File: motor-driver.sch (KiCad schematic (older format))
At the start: 9 parts, among them U3 A3950SLP-T

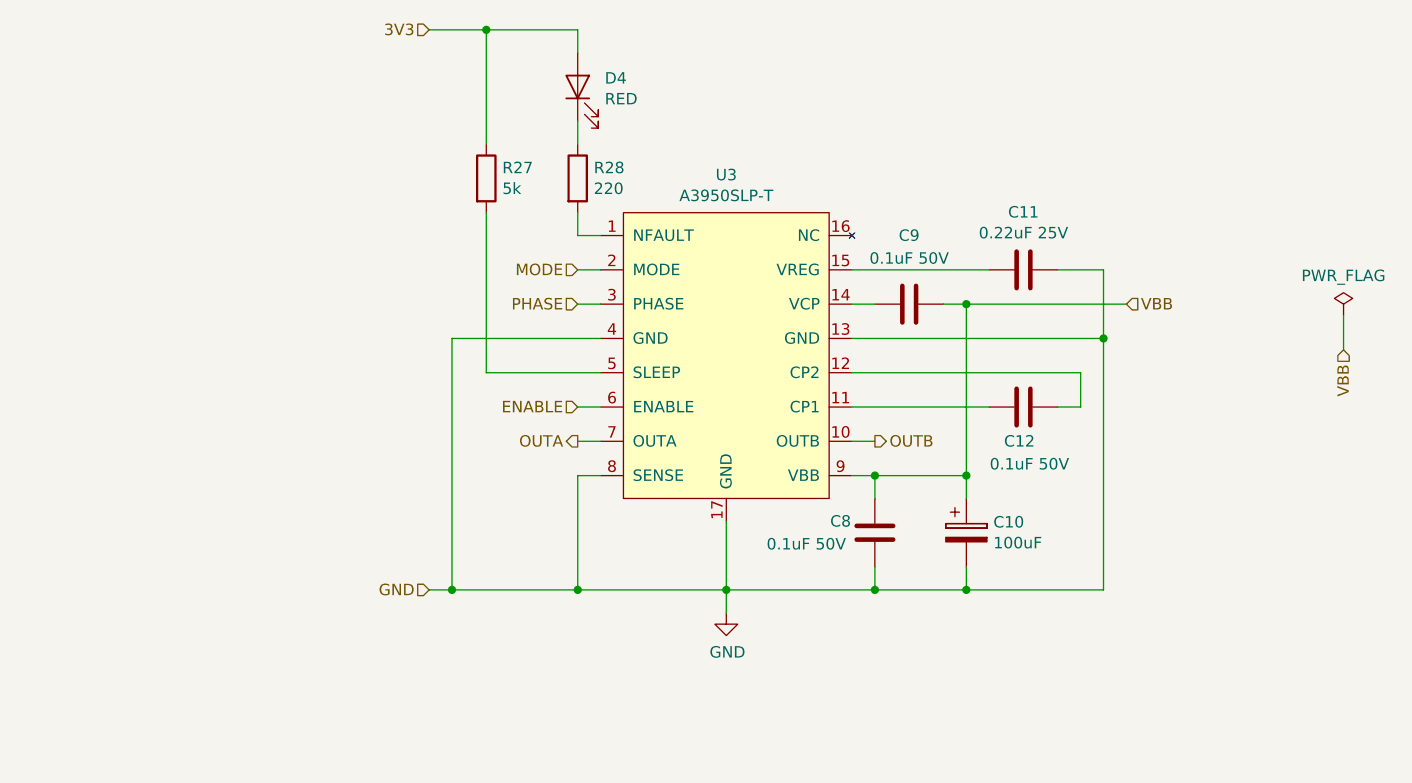
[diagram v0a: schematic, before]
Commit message: Generated annotations, netlists and assigned footprints into components
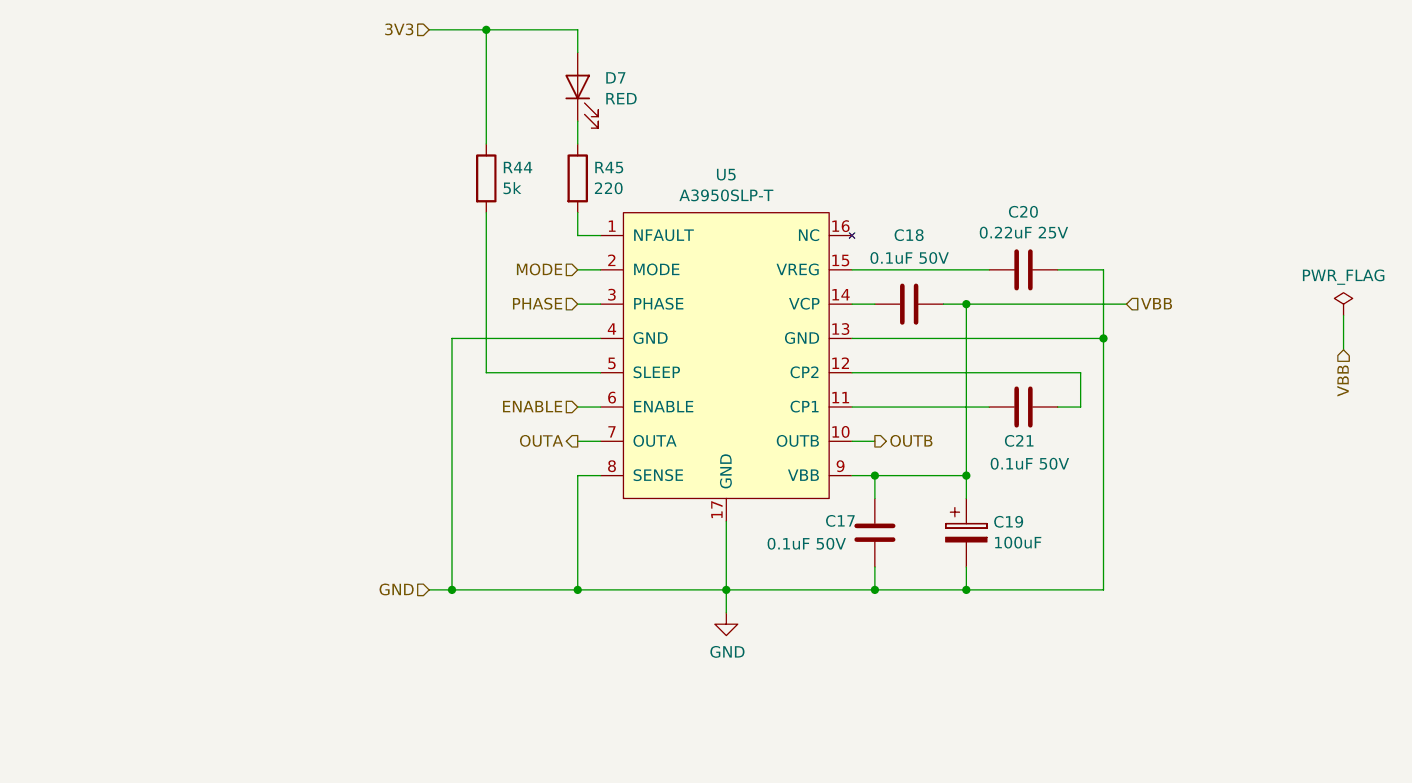
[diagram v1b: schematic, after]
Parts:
- C10: footprint (none) -> Capacitor_SMD:CP_Elec_8x10.5
- C11: footprint (none) -> Capacitor_SMD:C_0603_1608Metric_Pad1.05x0.95mm_HandSolder
- C12, C8, C9: footprint (none) -> Capacitor_SMD:C_0805_2012Metric_Pad1.15x1.40mm_HandSolder
- D4: footprint (none) -> LED_SMD:LED_0603_1608Metric_Pad1.05x0.95mm_HandSolder
- R27, R28: footprint (none) -> Resistor_SMD:R_0805_2012Metric_Pad1.15x1.40mm_HandSolder
- U3: footprint (none) -> Package_SO:HTSSOP-16-1EP_4.4x5mm_P0.65mm_EP3.4x5mm_Mask3x3mm_ThermalVias
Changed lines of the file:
@@
 AR Path="/5BF2FCBD/5BD9640D" Ref="U?"  Part="1"
 AR Path="/5C015BE4/5BD9640D" Ref="U5"  Part="1"
-F 0 "U3" H 6050 4415 50  0000 C CNN
+F 0 "U5" H 6050 4415 50  0000 C CNN
 F 1 "A3950SLP-T" H 6050 4324 50  0000 C CNN
-F 2 "" H 6100 4300 50  0001 C CNN
+F 2 "Package_SO:HTSSOP-16-1EP_4.4x5mm_P0.65mm_EP3.4x5mm_Mask3x3mm_ThermalVias" H 6100 4300 50  0001 C CNN
 F 3 "" H 6100 4300 50  0001 C CNN
 	1    5800 3600
@@
 AR Path="/5BF2FCBD/5BDA6B35" Ref="C?"  Part="1"
 AR Path="/5C015BE4/5BDA6B35" Ref="C17"  Part="1"
-F 0 "C8" H 6550 4400 50  0000 C CNN
+F 0 "C17" H 6550 4400 50  0000 C CNN
 F 1 "0.1uF 50V" H 6400 4300 50  0000 C CNN
-F 2 "" H 6738 4200 50  0001 C CNN
+F 2 "Capacitor_SMD:C_0805_2012Metric_Pad1.15x1.40mm_HandSolder" H 6738 4200 50  0001 C CNN
 F 3 "~" H 6700 4350 50  0001 C CNN
 F 4 "50V" V 6700 4350 50  0001 C CNN "Voltage"
@@
 AR Path="/5BF2FCBD/5BDBEA6E" Ref="C?"  Part="1"
 AR Path="/5C015BE4/5BDBEA6E" Ref="C21"  Part="1"
-F 0 "C12" V 7200 3750 50  0000 L CNN
+F 0 "C21" V 7200 3750 50  0000 L CNN
 F 1 "0.1uF 50V" V 7100 3600 50  0000 L CNN
-F 2 "" H 7388 3650 50  0001 C CNN
+F 2 "Capacitor_SMD:C_0805_2012Metric_Pad1.15x1.40mm_HandSolder" H 7388 3650 50  0001 C CNN
 F 3 "~" H 7350 3800 50  0001 C CNN
 	1    7350 3800
@@
 AR Path="/5BF2FCBD/5BDD7CCD" Ref="C?"  Part="1"
 AR Path="/5C015BE4/5BDD7CCD" Ref="C18"  Part="1"
-F 0 "C9" V 6550 3350 50  0000 C CNN
+F 0 "C18" V 6550 3350 50  0000 C CNN
 F 1 "0.1uF 50V" V 6650 3350 50  0000 C CNN
-F 2 "" H 6888 3200 50  0001 C CNN
+F 2 "Capacitor_SMD:C_0805_2012Metric_Pad1.15x1.40mm_HandSolder" H 6888 3200 50  0001 C CNN
 F 3 "~" H 6850 3350 50  0001 C CNN
 	1    6850 3350
@@
 AR Path="/5BF2FCBD/5BDE6995" Ref="C?"  Part="1"
 AR Path="/5C015BE4/5BDE6995" Ref="C19"  Part="1"
-F 0 "C10" H 7218 4396 50  0000 L CNN
+F 0 "C19" H 7218 4396 50  0000 L CNN
 F 1 "100uF" H 7218 4305 50  0000 L CNN
-F 2 "" H 7138 4200 50  0001 C CNN
+F 2 "Capacitor_SMD:CP_Elec_8x10.5" H 7138 4200 50  0001 C CNN
 F 3 "~" H 7100 4350 50  0001 C CNN
 	1    7100 4350
@@
 AR Path="/5BF2FCBD/5BDFF4AF" Ref="C?"  Part="1"
 AR Path="/5C015BE4/5BDFF4AF" Ref="C20"  Part="1"
-F 0 "C11" V 7098 3200 50  0000 C CNN
+F 0 "C20" V 7098 3200 50  0000 C CNN
 F 1 "0.22uF 25V" V 7189 3200 50  0000 C CNN
-F 2 "" H 7388 3050 50  0001 C CNN
+F 2 "Capacitor_SMD:C_0603_1608Metric_Pad1.05x0.95mm_HandSolder" H 7388 3050 50  0001 C CNN
 F 3 "~" H 7350 3200 50  0001 C CNN
 	1    7350 3200
@@
 AR Path="/5BF2FCBD/5BE2A012" Ref="R?"  Part="1"
 AR Path="/5C015BE4/5BE2A012" Ref="R44"  Part="1"
-F 0 "R27" H 5070 2846 50  0000 L CNN
+F 0 "R44" H 5070 2846 50  0000 L CNN
 F 1 "5k" H 5070 2755 50  0000 L CNN
-F 2 "" V 4930 2800 50  0001 C CNN
+F 2 "Resistor_SMD:R_0805_2012Metric_Pad1.15x1.40mm_HandSolder" V 4930 2800 50  0001 C CNN
 F 3 "~" H 5000 2800 50  0001 C CNN
 	1    5000 2800
@@
 AR Path="/5BF2FCBD/5BE427B2" Ref="D?"  Part="1"
 AR Path="/5C015BE4/5BE427B2" Ref="D7"  Part="1"
-F 0 "D4" V 5438 2282 50  0000 R CNN
+F 0 "D7" V 5438 2282 50  0000 R CNN
 F 1 "RED" V 5347 2282 50  0000 R CNN
-F 2 "" H 5400 2400 50  0001 C CNN
+F 2 "LED_SMD:LED_0603_1608Metric_Pad1.05x0.95mm_HandSolder" H 5400 2400 50  0001 C CNN
 F 3 "~" H 5400 2400 50  0001 C CNN
 	1    5400 2400
@@
 AR Path="/5BF2FCBD/5BE42954" Ref="R?"  Part="1"
 AR Path="/5C015BE4/5BE42954" Ref="R45"  Part="1"
-F 0 "R28" H 5470 2846 50  0000 L CNN
+F 0 "R45" H 5470 2846 50  0000 L CNN
 F 1 "220" H 5470 2755 50  0000 L CNN
-F 2 "" V 5330 2800 50  0001 C CNN
+F 2 "Resistor_SMD:R_0805_2012Metric_Pad1.15x1.40mm_HandSolder" V 5330 2800 50  0001 C CNN
 F 3 "~" H 5400 2800 50  0001 C CNN
 	1    5400 2800

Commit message: Added power supply section to PCB. Added missing components footprints.
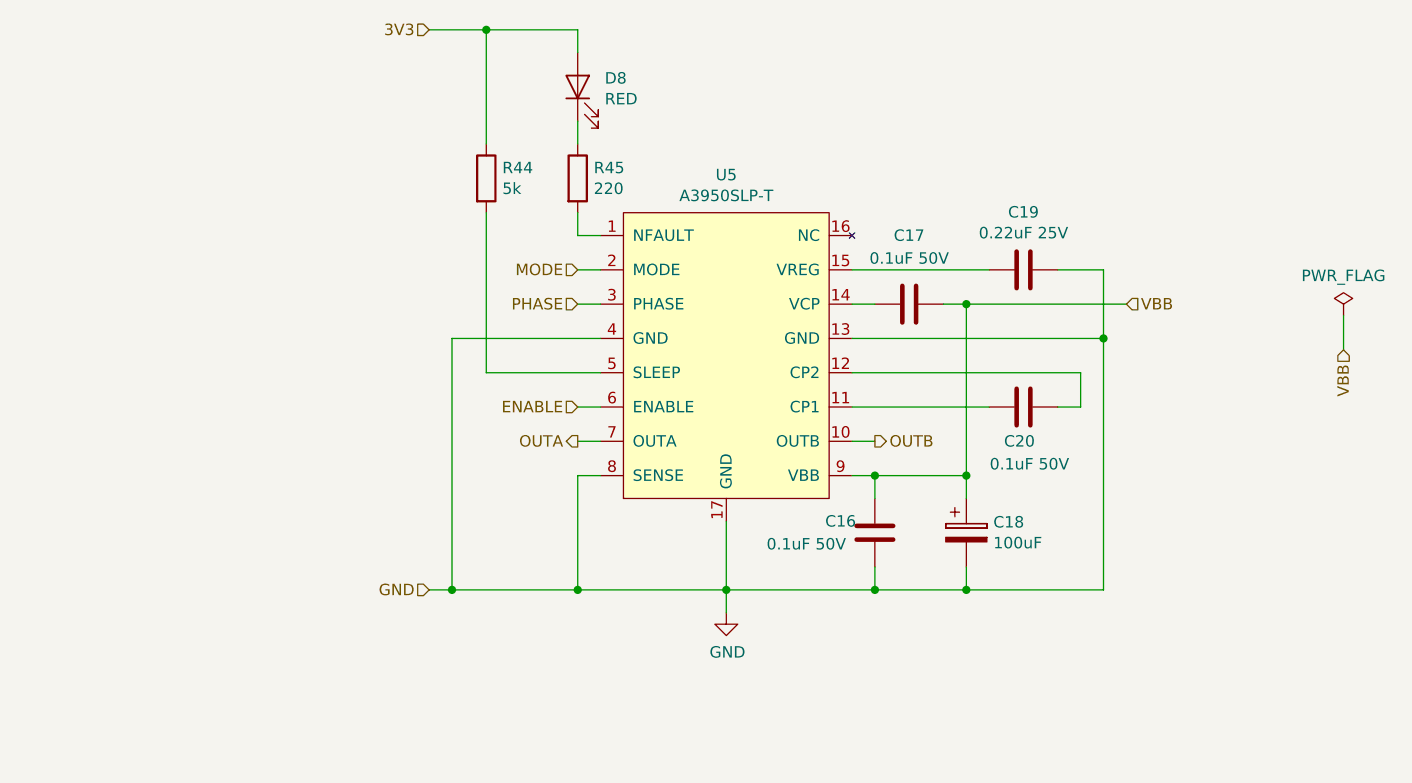
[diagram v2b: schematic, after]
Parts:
- renumbered C11 to C10, C12 to C11, C8 to C7, C9 to C8, C10 to C9, D4 to D5
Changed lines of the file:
@@
 $EndComp
 $Comp
-L power:GND #PWR017
+L power:GND #PWR010
 U 1 1 5BD9C7A2
 P 6050 4700
-AR Path="/5BDB64FF/5BD9C7A2" Ref="#PWR017"  Part="1"
+AR Path="/5BDB64FF/5BD9C7A2" Ref="#PWR010"  Part="1"
 AR Path="/5BF2FCBD/5BD9C7A2" Ref="#PWR?"  Part="1"
-AR Path="/5C015BE4/5BD9C7A2" Ref="#PWR023"  Part="1"
-F 0 "#PWR023" H 6050 4450 50  0001 C CNN
+AR Path="/5C015BE4/5BD9C7A2" Ref="#PWR014"  Part="1"
+F 0 "#PWR014" H 6050 4450 50  0001 C CNN
 F 1 "GND" H 6055 4527 50  0000 C CNN
 F 2 "" H 6050 4700 50  0001 C CNN
@@
 	5400 4600 4850 4600
 $Comp
-L Device:C C8
+L Device:C C7
 U 1 1 5BDA6B35
 P 6700 4350
-AR Path="/5BDB64FF/5BDA6B35" Ref="C8"  Part="1"
+AR Path="/5BDB64FF/5BDA6B35" Ref="C7"  Part="1"
 AR Path="/5BF2FCBD/5BDA6B35" Ref="C?"  Part="1"
-AR Path="/5C015BE4/5BDA6B35" Ref="C17"  Part="1"
-F 0 "C17" H 6550 4400 50  0000 C CNN
+AR Path="/5C015BE4/5BDA6B35" Ref="C16"  Part="1"
+F 0 "C16" H 6550 4400 50  0000 C CNN
 F 1 "0.1uF 50V" H 6400 4300 50  0000 C CNN
 F 2 "Capacitor_SMD:C_0805_2012Metric_Pad1.15x1.40mm_HandSolder" H 6738 4200 50  0001 C CNN
@@
 	6600 4100 6700 4100
 $Comp
-L Device:C C12
+L Device:C C11
 U 1 1 5BDBEA6E
 P 7350 3800
-AR Path="/5BDB64FF/5BDBEA6E" Ref="C12"  Part="1"
+AR Path="/5BDB64FF/5BDBEA6E" Ref="C11"  Part="1"
 AR Path="/5BF2FCBD/5BDBEA6E" Ref="C?"  Part="1"
-AR Path="/5C015BE4/5BDBEA6E" Ref="C21"  Part="1"
-F 0 "C21" V 7200 3750 50  0000 L CNN
+AR Path="/5C015BE4/5BDBEA6E" Ref="C20"  Part="1"
+F 0 "C20" V 7200 3750 50  0000 L CNN
 F 1 "0.1uF 50V" V 7100 3600 50  0000 L CNN
 F 2 "Capacitor_SMD:C_0805_2012Metric_Pad1.15x1.40mm_HandSolder" H 7388 3650 50  0001 C CNN
@@
 	6700 4600 6700 4500
 $Comp
-L Device:C C9
+L Device:C C8
 U 1 1 5BDD7CCD
 P 6850 3350
-AR Path="/5BDB64FF/5BDD7CCD" Ref="C9"  Part="1"
+AR Path="/5BDB64FF/5BDD7CCD" Ref="C8"  Part="1"
 AR Path="/5BF2FCBD/5BDD7CCD" Ref="C?"  Part="1"
-AR Path="/5C015BE4/5BDD7CCD" Ref="C18"  Part="1"
-F 0 "C18" V 6550 3350 50  0000 C CNN
+AR Path="/5C015BE4/5BDD7CCD" Ref="C17"  Part="1"
+F 0 "C17" V 6550 3350 50  0000 C CNN
 F 1 "0.1uF 50V" V 6650 3350 50  0000 C CNN
 F 2 "Capacitor_SMD:C_0805_2012Metric_Pad1.15x1.40mm_HandSolder" H 6888 3200 50  0001 C CNN
@@
 Connection ~ 6700 4600
 $Comp
-L Device:CP C10
+L Device:CP C9
 U 1 1 5BDE6995
 P 7100 4350
-AR Path="/5BDB64FF/5BDE6995" Ref="C10"  Part="1"
+AR Path="/5BDB64FF/5BDE6995" Ref="C9"  Part="1"
 AR Path="/5BF2FCBD/5BDE6995" Ref="C?"  Part="1"
-AR Path="/5C015BE4/5BDE6995" Ref="C19"  Part="1"
-F 0 "C19" H 7218 4396 50  0000 L CNN
+AR Path="/5C015BE4/5BDE6995" Ref="C18"  Part="1"
+F 0 "C18" H 7218 4396 50  0000 L CNN
 F 1 "100uF" H 7218 4305 50  0000 L CNN
 F 2 "Capacitor_SMD:CP_Elec_8x10.5" H 7138 4200 50  0001 C CNN
@@
 Connection ~ 7100 4600
 $Comp
-L Device:C C11
+L Device:C C10
 U 1 1 5BDFF4AF
 P 7350 3200
-AR Path="/5BDB64FF/5BDFF4AF" Ref="C11"  Part="1"
+AR Path="/5BDB64FF/5BDFF4AF" Ref="C10"  Part="1"
 AR Path="/5BF2FCBD/5BDFF4AF" Ref="C?"  Part="1"
-AR Path="/5C015BE4/5BDFF4AF" Ref="C20"  Part="1"
-F 0 "C20" V 7098 3200 50  0000 C CNN
+AR Path="/5C015BE4/5BDFF4AF" Ref="C19"  Part="1"
+F 0 "C19" V 7098 3200 50  0000 C CNN
 F 1 "0.22uF 25V" V 7189 3200 50  0000 C CNN
 F 2 "Capacitor_SMD:C_0603_1608Metric_Pad1.05x0.95mm_HandSolder" H 7388 3050 50  0001 C CNN
@@
 	5000 3650 5500 3650
 $Comp
-L Device:LED D4
+L Device:LED D5
 U 1 1 5BE427B2
 P 5400 2400
-AR Path="/5BDB64FF/5BE427B2" Ref="D4"  Part="1"
+AR Path="/5BDB64FF/5BE427B2" Ref="D5"  Part="1"
 AR Path="/5BF2FCBD/5BE427B2" Ref="D?"  Part="1"
-AR Path="/5C015BE4/5BE427B2" Ref="D7"  Part="1"
-F 0 "D7" V 5438 2282 50  0000 R CNN
+AR Path="/5C015BE4/5BE427B2" Ref="D8"  Part="1"
+F 0 "D8" V 5438 2282 50  0000 R CNN
 F 1 "RED" V 5347 2282 50  0000 R CNN
 F 2 "LED_SMD:LED_0603_1608Metric_Pad1.05x0.95mm_HandSolder" H 5400 2400 50  0001 C CNN
@@
 VBB
 $Comp
-L power:PWR_FLAG #FLG02
+L power:PWR_FLAG #FLG03
 U 1 1 5C04A11D
 P 8750 3400
-AR Path="/5BDB64FF/5C04A11D" Ref="#FLG02"  Part="1"
-AR Path="/5C015BE4/5C04A11D" Ref="#FLG03"  Part="1"
-F 0 "#FLG03" H 8750 3475 50  0001 C CNN
+AR Path="/5BDB64FF/5C04A11D" Ref="#FLG03"  Part="1"
+AR Path="/5C015BE4/5C04A11D" Ref="#FLG04"  Part="1"
+F 0 "#FLG04" H 8750 3475 50  0001 C CNN
 F 1 "PWR_FLAG" H 8750 3574 50  0000 C CNN
 F 2 "" H 8750 3400 50  0001 C CNN

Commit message: PCB creation, improvements of power supply section
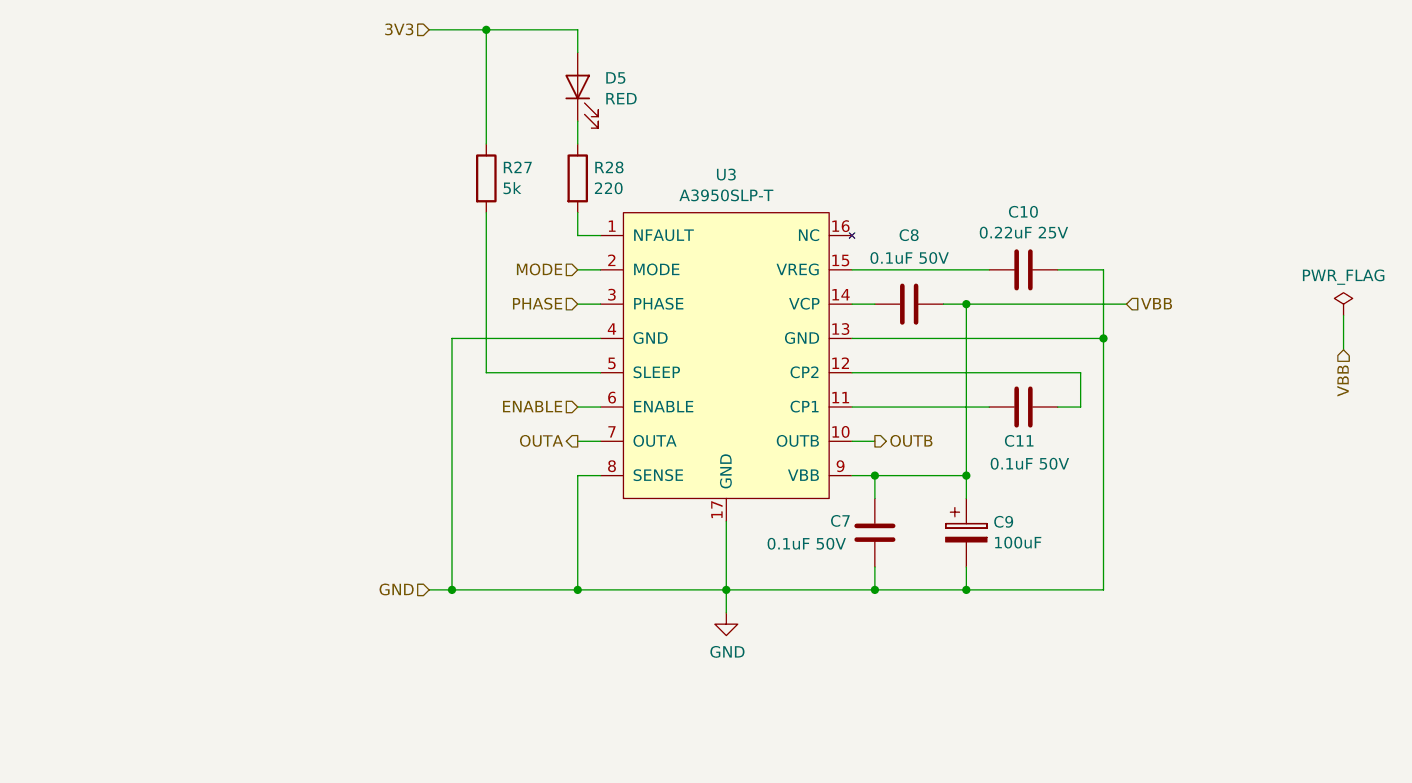
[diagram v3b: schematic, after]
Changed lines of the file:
@@
 AR Path="/5BF2FCBD/5BD9640D" Ref="U?"  Part="1"
 AR Path="/5C015BE4/5BD9640D" Ref="U5"  Part="1"
-F 0 "U5" H 6050 4415 50  0000 C CNN
+F 0 "U3" H 6050 4415 50  0000 C CNN
 F 1 "A3950SLP-T" H 6050 4324 50  0000 C CNN
 F 2 "Package_SO:HTSSOP-16-1EP_4.4x5mm_P0.65mm_EP3.4x5mm_Mask3x3mm_ThermalVias" H 6100 4300 50  0001 C CNN
@@
 AR Path="/5BF2FCBD/5BDA6B35" Ref="C?"  Part="1"
 AR Path="/5C015BE4/5BDA6B35" Ref="C16"  Part="1"
-F 0 "C16" H 6550 4400 50  0000 C CNN
+F 0 "C7" H 6550 4400 50  0000 C CNN
 F 1 "0.1uF 50V" H 6400 4300 50  0000 C CNN
 F 2 "Capacitor_SMD:C_0805_2012Metric_Pad1.15x1.40mm_HandSolder" H 6738 4200 50  0001 C CNN
@@
 AR Path="/5BF2FCBD/5BDBEA6E" Ref="C?"  Part="1"
 AR Path="/5C015BE4/5BDBEA6E" Ref="C20"  Part="1"
-F 0 "C20" V 7200 3750 50  0000 L CNN
+F 0 "C11" V 7200 3750 50  0000 L CNN
 F 1 "0.1uF 50V" V 7100 3600 50  0000 L CNN
 F 2 "Capacitor_SMD:C_0805_2012Metric_Pad1.15x1.40mm_HandSolder" H 7388 3650 50  0001 C CNN
@@
 AR Path="/5BF2FCBD/5BDD7CCD" Ref="C?"  Part="1"
 AR Path="/5C015BE4/5BDD7CCD" Ref="C17"  Part="1"
-F 0 "C17" V 6550 3350 50  0000 C CNN
+F 0 "C8" V 6550 3350 50  0000 C CNN
 F 1 "0.1uF 50V" V 6650 3350 50  0000 C CNN
 F 2 "Capacitor_SMD:C_0805_2012Metric_Pad1.15x1.40mm_HandSolder" H 6888 3200 50  0001 C CNN
@@
 AR Path="/5BF2FCBD/5BDE6995" Ref="C?"  Part="1"
 AR Path="/5C015BE4/5BDE6995" Ref="C18"  Part="1"
-F 0 "C18" H 7218 4396 50  0000 L CNN
+F 0 "C9" H 7218 4396 50  0000 L CNN
 F 1 "100uF" H 7218 4305 50  0000 L CNN
 F 2 "Capacitor_SMD:CP_Elec_8x10.5" H 7138 4200 50  0001 C CNN
@@
 AR Path="/5BF2FCBD/5BDFF4AF" Ref="C?"  Part="1"
 AR Path="/5C015BE4/5BDFF4AF" Ref="C19"  Part="1"
-F 0 "C19" V 7098 3200 50  0000 C CNN
+F 0 "C10" V 7098 3200 50  0000 C CNN
 F 1 "0.22uF 25V" V 7189 3200 50  0000 C CNN
 F 2 "Capacitor_SMD:C_0603_1608Metric_Pad1.05x0.95mm_HandSolder" H 7388 3050 50  0001 C CNN
@@
 AR Path="/5BF2FCBD/5BE2A012" Ref="R?"  Part="1"
 AR Path="/5C015BE4/5BE2A012" Ref="R44"  Part="1"
-F 0 "R44" H 5070 2846 50  0000 L CNN
+F 0 "R27" H 5070 2846 50  0000 L CNN
 F 1 "5k" H 5070 2755 50  0000 L CNN
 F 2 "Resistor_SMD:R_0805_2012Metric_Pad1.15x1.40mm_HandSolder" V 4930 2800 50  0001 C CNN
@@
 AR Path="/5BF2FCBD/5BE427B2" Ref="D?"  Part="1"
 AR Path="/5C015BE4/5BE427B2" Ref="D8"  Part="1"
-F 0 "D8" V 5438 2282 50  0000 R CNN
+F 0 "D5" V 5438 2282 50  0000 R CNN
 F 1 "RED" V 5347 2282 50  0000 R CNN
 F 2 "LED_SMD:LED_0603_1608Metric_Pad1.05x0.95mm_HandSolder" H 5400 2400 50  0001 C CNN
@@
 AR Path="/5BF2FCBD/5BE42954" Ref="R?"  Part="1"
 AR Path="/5C015BE4/5BE42954" Ref="R45"  Part="1"
-F 0 "R45" H 5470 2846 50  0000 L CNN
+F 0 "R28" H 5470 2846 50  0000 L CNN
 F 1 "220" H 5470 2755 50  0000 L CNN
 F 2 "Resistor_SMD:R_0805_2012Metric_Pad1.15x1.40mm_HandSolder" V 5330 2800 50  0001 C CNN
